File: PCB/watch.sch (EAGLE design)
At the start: 58 parts, among them IC1 ISL1209, J2 USB-MICROB, Q1 32.768 KHz, T1 BC850, U2 MKL27Z256VLH4

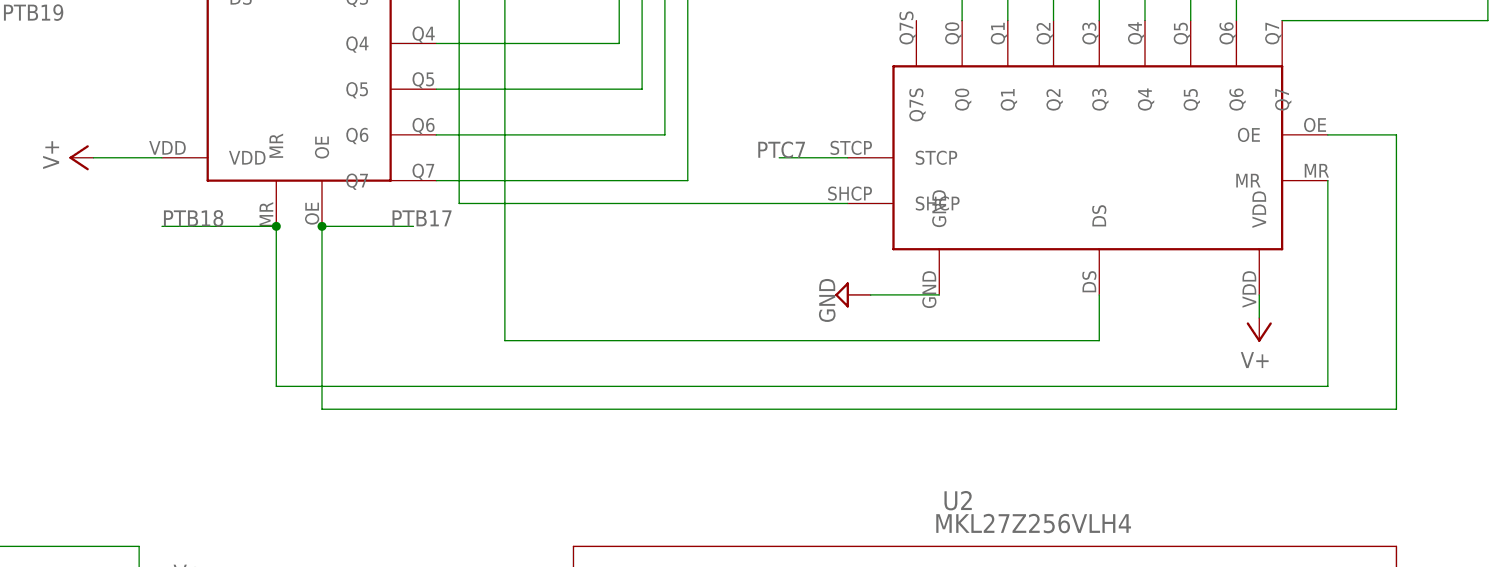
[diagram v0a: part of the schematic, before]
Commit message: wired all SR but one pin
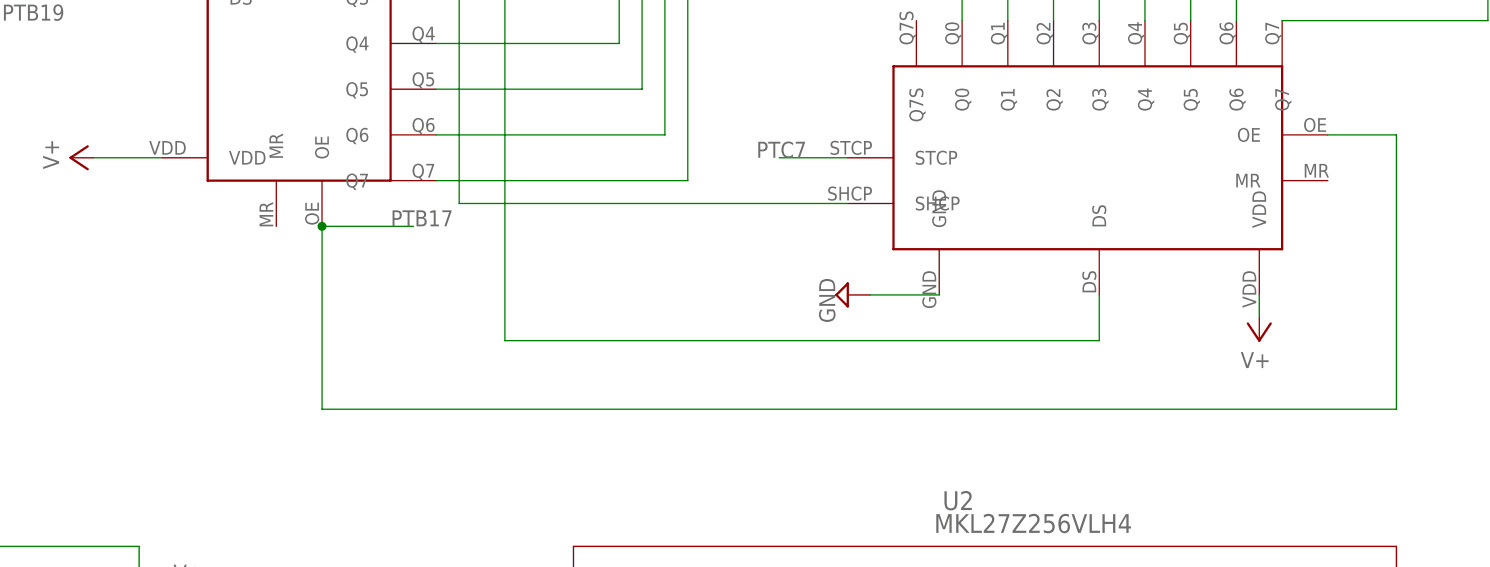
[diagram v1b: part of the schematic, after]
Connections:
- net PTB18: no longer U$4.MR, U$5.MR
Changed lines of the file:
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@@
 <net name="PTB18" class="0">
-<segment>
-<pinref part="U$5" gate="G$1" pin="MR"/>
-<wire x1="66.04" y1="208.28" x2="66.04" y2="185.42" width="0.1524" layer="91"/>
-<pinref part="U$4" gate="G$1" pin="MR"/>
-<wire x1="66.04" y1="185.42" x2="-50.8" y2="185.42" width="0.1524" layer="91"/>
-<wire x1="-50.8" y1="185.42" x2="-50.8" y2="203.2" width="0.1524" layer="91"/>
-<wire x1="-50.8" y1="203.2" x2="-63.5" y2="203.2" width="0.1524" layer="91"/>
-<junction x="-50.8" y="203.2"/>
-<label x="-63.5" y="203.2" size="1.778" layer="95"/>
-</segment>
 <segment>
 <pinref part="U2" gate="A" pin="PTB18"/>

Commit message: moved clock, rewired gps
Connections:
- net PTB3: no longer U1.3D-FIX
- net PTD3: now also U1.3D-FIX
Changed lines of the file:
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@@
 <junction x="88.9" y="96.52"/>
-</segment>
-<segment>
-<pinref part="U1" gate="G$1" pin="3D-FIX"/>
-<wire x1="162.56" y1="91.44" x2="149.86" y2="91.44" width="0.1524" layer="91"/>
-<label x="149.86" y="88.9" size="1.778" layer="95"/>
 </segment>
 </net>
@@
 <label x="-142.24" y="58.42" size="1.778" layer="95"/>
 </segment>
-</net>
+<segment>
+<pinref part="U1" gate="G$1" pin="3D-FIX"/>
+<wire x1="162.56" y1="91.44" x2="152.4" y2="91.44" width="0.1524" layer="91"/>
+</segment>
+</net>

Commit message: rewired gps
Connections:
- new net PTC10: U1.3D-FIX, U2.PTC10
- new net PTC11: U1.TX, U2.PTC11
- net PTA19: no longer U1.TX
- net PTD3: no longer U1.3D-FIX
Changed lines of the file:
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@@
 <junction x="83.82" y="83.82"/>
-</segment>
-<segment>
-<pinref part="U1" gate="G$1" pin="TX"/>
-<wire x1="162.56" y1="81.28" x2="152.4" y2="81.28" width="0.1524" layer="91"/>
-<label x="149.86" y="81.28" size="1.778" layer="95"/>
 </segment>
 </net>
@@
 <label x="-142.24" y="58.42" size="1.778" layer="95"/>
 </segment>
-<segment>
-<pinref part="U1" gate="G$1" pin="3D-FIX"/>
-<wire x1="162.56" y1="91.44" x2="152.4" y2="91.44" width="0.1524" layer="91"/>
-</segment>
 </net>
 <net name="PTD2" class="0">
@@
 </segment>
 </net>
+<net name="PTC10" class="0">
+<segment>
+<pinref part="U1" gate="G$1" pin="3D-FIX"/>
+<wire x1="162.56" y1="91.44" x2="152.4" y2="91.44" width="0.1524" layer="91"/>
+<label x="149.86" y="88.9" size="1.778" layer="95"/>
+</segment>
+<segment>
+<pinref part="U2" gate="A" pin="PTC10"/>
+<wire x1="81.28" y1="139.7" x2="86.36" y2="139.7" width="0.1524" layer="91"/>
+<junction x="86.36" y="139.7"/>
+</segment>
+</net>
+<net name="PTC11" class="0">
+<segment>
+<pinref part="U1" gate="G$1" pin="TX"/>
+<wire x1="162.56" y1="81.28" x2="152.4" y2="81.28" width="0.1524" layer="91"/>
+<label x="149.86" y="78.74" size="1.778" layer="95"/>
+</segment>
+<segment>
+<pinref part="U2" gate="A" pin="PTC11"/>
+<wire x1="81.28" y1="142.24" x2="86.36" y2="142.24" width="0.1524" layer="91"/>
+<junction x="86.36" y="142.24"/>
+</segment>
+</net>

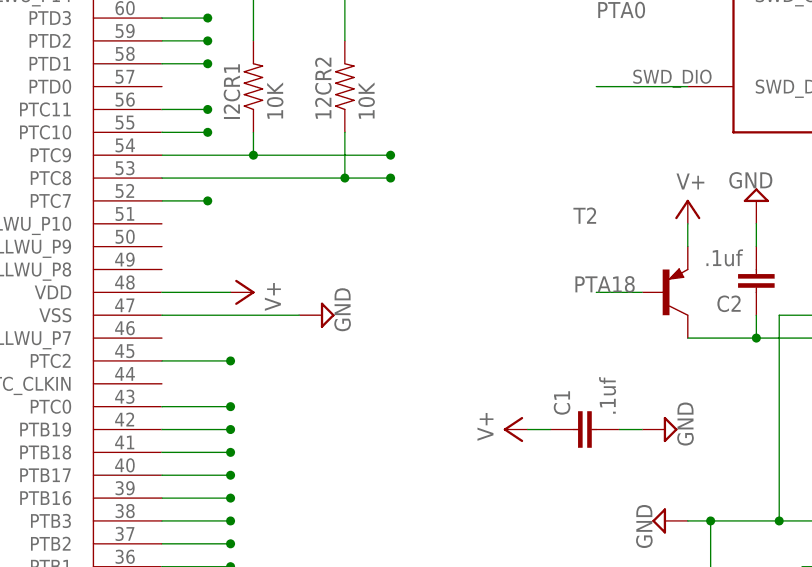
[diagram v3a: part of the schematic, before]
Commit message: removed airwires, added decoupling caps
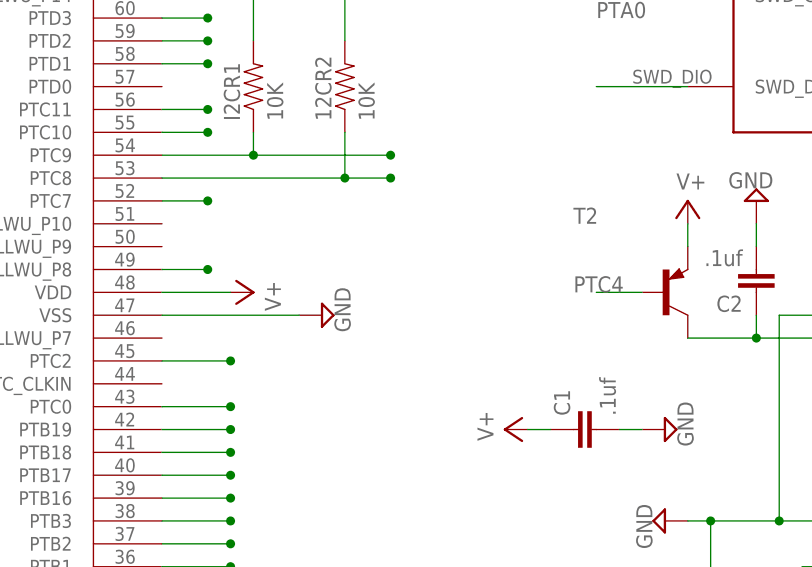
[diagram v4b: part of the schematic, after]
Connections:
- new net PTC4: T2.B, U2.PTC4/LLWU_P8
- net PTA18: no longer T2.B
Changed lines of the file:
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@@
 <junction x="-33.02" y="83.82"/>
-</segment>
-<segment>
-<pinref part="T2" gate="G$1" pin="B"/>
-<wire x1="134.62" y1="121.92" x2="129.54" y2="121.92" width="0.1524" layer="91"/>
-<label x="127" y="121.92" size="1.778" layer="95"/>
 </segment>
 </net>
@@
 </segment>
 </net>
+<net name="PTC4" class="0">
+<segment>
+<pinref part="U2" gate="A" pin="PTC4/LLWU_P8"/>
+<wire x1="81.28" y1="124.46" x2="86.36" y2="124.46" width="0.1524" layer="91"/>
+<junction x="86.36" y="124.46"/>
+</segment>
+<segment>
+<pinref part="T2" gate="G$1" pin="B"/>
+<wire x1="134.62" y1="121.92" x2="129.54" y2="121.92" width="0.1524" layer="91"/>
+<label x="127" y="121.92" size="1.778" layer="95"/>
+</segment>
+</net>

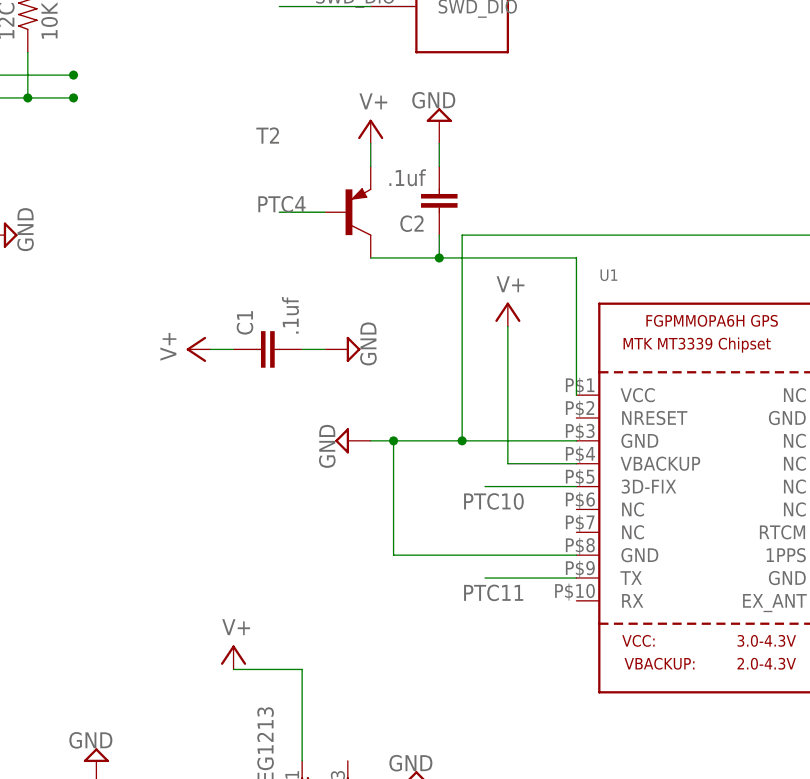
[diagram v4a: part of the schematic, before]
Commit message: added gps tx resistor
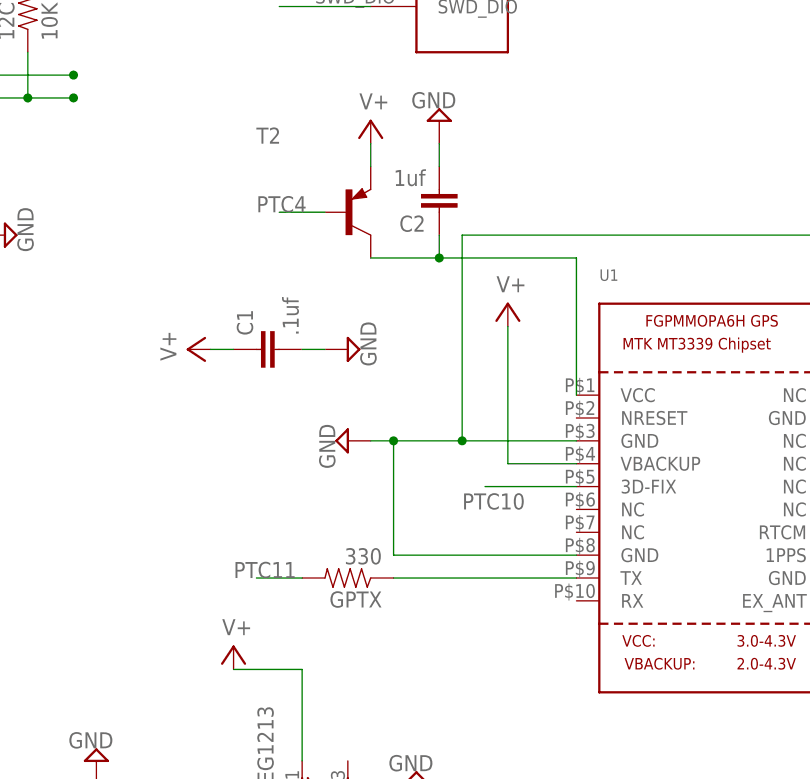
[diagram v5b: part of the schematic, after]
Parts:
- added GPTX: 330, SparkFun-Resistors:RESISTOR0603
- C2: value .1uf -> 1uf
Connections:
- new net N$30: GPTX.1, U1.TX
- net PTC11: now also GPTX.2; no longer U1.TX
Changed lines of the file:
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@@
 <part name="SUPPLY6" library="supply2" deviceset="GND" device=""/>
 <part name="SUPPLY7" library="supply2" deviceset="GND" device=""/>
-<part name="C2" library="SparkFun" deviceset="CAP" device="0603" value=".1uf"/>
+<part name="C2" library="SparkFun" deviceset="CAP" device="0603" value="1uf"/>
 <part name="SUPPLY10" library="supply2" deviceset="V+" device=""/>
 <part name="U$3" library="5-wayswitch" deviceset="5-WAYSWITCH" device=""/>
@@
 <part name="R9" library="SparkFun-Resistors" deviceset="RESISTOR" device="0603" value="680"/>
 <part name="R10" library="SparkFun-Resistors" deviceset="RESISTOR" device="0603" value="680"/>
+<part name="GPTX" library="SparkFun-Resistors" deviceset="RESISTOR" device="0603" value="330"/>
 </parts>
 <sheets>
@@
 <instance part="R9" gate="G$1" x="81.28" y="269.24" rot="R270"/>
 <instance part="R10" gate="G$1" x="83.82" y="259.08" rot="R270"/>
+<instance part="GPTX" gate="G$1" x="137.16" y="81.28" rot="R180"/>
 </instances>
 <busses>
@@
 <net name="PTC11" class="0">
 <segment>
-<pinref part="U1" gate="G$1" pin="TX"/>
-<wire x1="162.56" y1="81.28" x2="152.4" y2="81.28" width="0.1524" layer="91"/>
-<label x="149.86" y="78.74" size="1.778" layer="95"/>
-</segment>
-<segment>
 <pinref part="U2" gate="A" pin="PTC11"/>
 <wire x1="81.28" y1="142.24" x2="86.36" y2="142.24" width="0.1524" layer="91"/>
 <junction x="86.36" y="142.24"/>
 </segment>
+<segment>
+<pinref part="GPTX" gate="G$1" pin="2"/>
+<wire x1="132.08" y1="81.28" x2="127" y2="81.28" width="0.1524" layer="91"/>
+<label x="124.46" y="81.28" size="1.778" layer="95"/>
+</segment>
 </net>
 <net name="PTC4" class="0">
@@
 </segment>
 </net>
+<net name="N$30" class="0">
+<segment>
+<pinref part="GPTX" gate="G$1" pin="1"/>
+<pinref part="U1" gate="G$1" pin="TX"/>
+<wire x1="142.24" y1="81.28" x2="162.56" y2="81.28" width="0.1524" layer="91"/>
+</segment>
+</net>

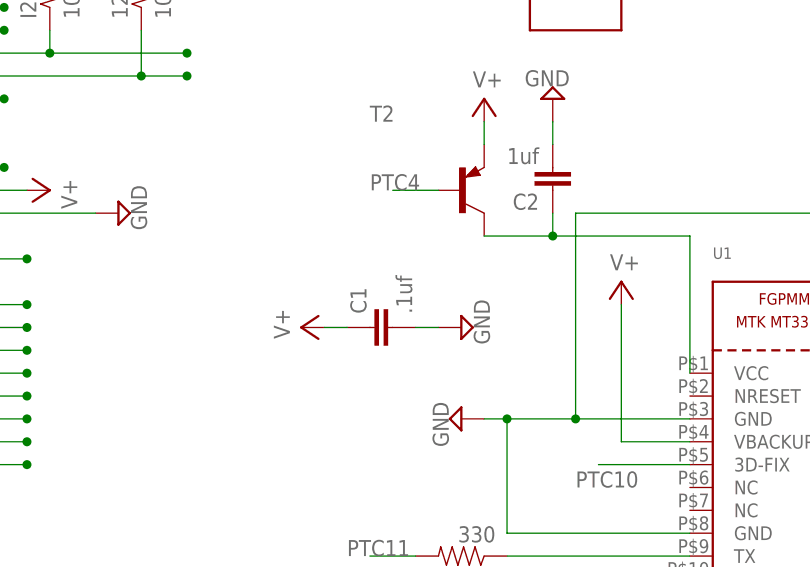
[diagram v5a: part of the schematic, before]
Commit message: altered values on gps caps
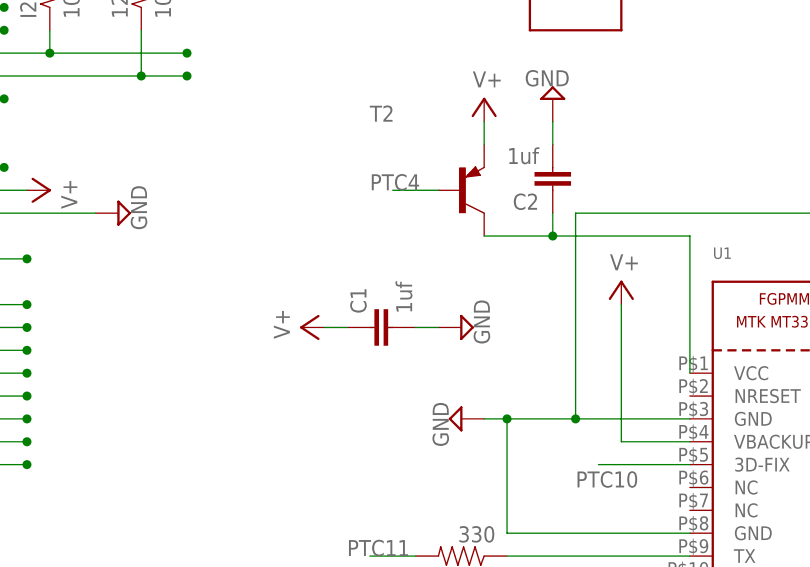
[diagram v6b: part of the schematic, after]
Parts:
- C1: value .1uf -> 1uf
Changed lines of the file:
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@@
 <part name="T2" library="transistor" deviceset="*-PNP-" device="SOT23-EBC"/>
 <part name="SUPPLY32" library="supply2" deviceset="V+" device=""/>
-<part name="C1" library="SparkFun" deviceset="CAP" device="0603" value=".1uf"/>
+<part name="C1" library="SparkFun" deviceset="CAP" device="0603" value="1uf"/>
 <part name="SUPPLY8" library="supply2" deviceset="V+" device=""/>
 <part name="SUPPLY9" library="supply2" deviceset="GND" device=""/>

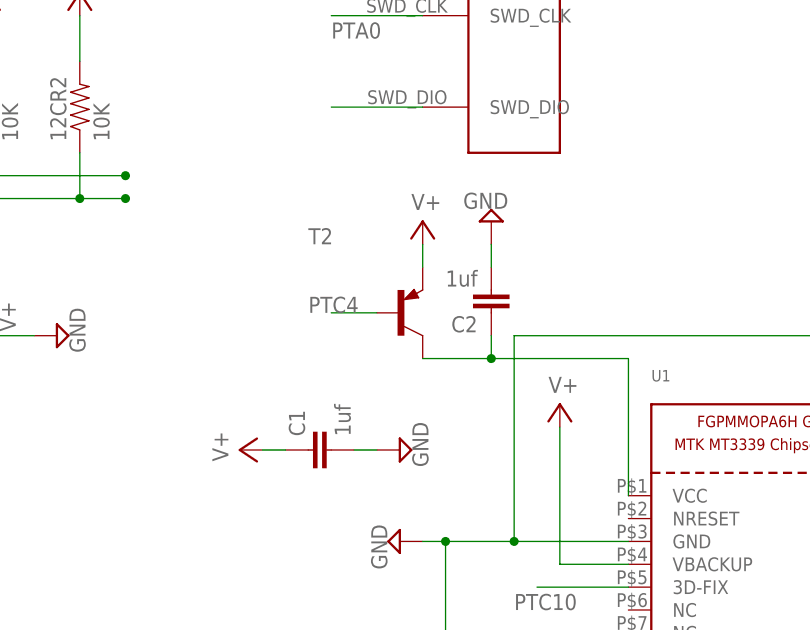
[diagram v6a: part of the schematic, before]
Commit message: finished adding gps caps per https://cdn-shop.adafruit.com/datasheets/GlobalTop-FGPMMOPA6H-Datasheet-V0A.pdf page 26
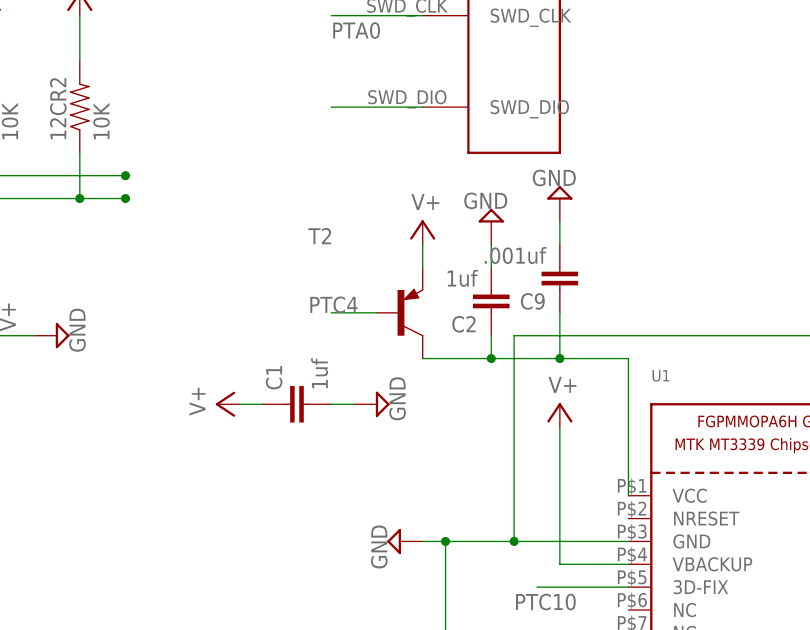
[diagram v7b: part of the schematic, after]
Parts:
- added C9: .001uf, SparkFun:CAP0603
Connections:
- net GND: now also C9.2
- net N$6: now also C9.1
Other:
- moved on the sheet: C1
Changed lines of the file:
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@@
 <part name="R10" library="SparkFun-Resistors" deviceset="RESISTOR" device="0603" value="680"/>
 <part name="GPTX" library="SparkFun-Resistors" deviceset="RESISTOR" device="0603" value="330"/>
+<part name="C9" library="SparkFun" deviceset="CAP" device="0603" value=".001uf"/>
+<part name="SUPPLY43" library="supply2" deviceset="GND" device=""/>
 </parts>
 <sheets>
@@
 <instance part="T2" gate="G$1" x="137.16" y="121.92"/>
 <instance part="SUPPLY32" gate="1" x="139.7" y="132.08"/>
-<instance part="C1" gate="G$1" x="129.54" y="106.68" rot="R90"/>
-<instance part="SUPPLY8" gate="1" x="119.38" y="106.68" rot="R90"/>
-<instance part="SUPPLY9" gate="GND" x="137.16" y="106.68" rot="R90"/>
+<instance part="C1" gate="G$1" x="127" y="111.76" rot="R90"/>
+<instance part="SUPPLY8" gate="1" x="116.84" y="111.76" rot="R90"/>
+<instance part="SUPPLY9" gate="GND" x="134.62" y="111.76" rot="R90"/>
 <instance part="SUPPLY33" gate="GND" x="147.32" y="132.08" rot="R180"/>
 <instance part="SUPPLY34" gate="GND" x="-35.56" y="154.94" rot="R270"/>
@@
 <instance part="R10" gate="G$1" x="83.82" y="259.08" rot="R270"/>
 <instance part="GPTX" gate="G$1" x="137.16" y="81.28" rot="R180"/>
+<instance part="C9" gate="G$1" x="154.94" y="127" rot="R180"/>
+<instance part="SUPPLY43" gate="GND" x="154.94" y="134.62" rot="R180"/>
 </instances>
 <busses>
@@
 <pinref part="C1" gate="G$1" pin="2"/>
 <pinref part="SUPPLY9" gate="GND" pin="GND"/>
-<wire x1="132.08" y1="106.68" x2="134.62" y2="106.68" width="0.1524" layer="91"/>
+<wire x1="129.54" y1="111.76" x2="132.08" y2="111.76" width="0.1524" layer="91"/>
 </segment>
 <segment>
@@
 <junction x="111.76" y="193.04"/>
 </segment>
+<segment>
+<pinref part="C9" gate="G$1" pin="2"/>
+<pinref part="SUPPLY43" gate="GND" pin="GND"/>
+<wire x1="154.94" y1="129.54" x2="154.94" y2="132.08" width="0.1524" layer="91"/>
+</segment>
 </net>
 <net name="V+" class="0">
@@
 <pinref part="C1" gate="G$1" pin="1"/>
 <pinref part="SUPPLY8" gate="1" pin="V+"/>
-<wire x1="124.46" y1="106.68" x2="121.92" y2="106.68" width="0.1524" layer="91"/>
+<wire x1="121.92" y1="111.76" x2="119.38" y2="111.76" width="0.1524" layer="91"/>
 </segment>
 <segment>
@@
 <wire x1="162.56" y1="101.6" x2="162.56" y2="116.84" width="0.1524" layer="91"/>
 <pinref part="T2" gate="G$1" pin="C"/>
-<wire x1="162.56" y1="116.84" x2="147.32" y2="116.84" width="0.1524" layer="91"/>
+<wire x1="162.56" y1="116.84" x2="154.94" y2="116.84" width="0.1524" layer="91"/>
 <pinref part="C2" gate="G$1" pin="1"/>
+<wire x1="154.94" y1="116.84" x2="147.32" y2="116.84" width="0.1524" layer="91"/>
 <wire x1="147.32" y1="116.84" x2="139.7" y2="116.84" width="0.1524" layer="91"/>
 <wire x1="147.32" y1="116.84" x2="147.32" y2="119.38" width="0.1524" layer="91"/>
 <junction x="147.32" y="116.84"/>
+<pinref part="C9" gate="G$1" pin="1"/>
+<wire x1="154.94" y1="121.92" x2="154.94" y2="116.84" width="0.1524" layer="91"/>
+<junction x="154.94" y="116.84"/>
 </segment>
 </net>
